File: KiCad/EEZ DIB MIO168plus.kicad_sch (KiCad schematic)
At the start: 11 parts

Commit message: BOM update
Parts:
- KK1, KK2: LCSC (none) -> C959626
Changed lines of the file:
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@@
 	(title_block
 		(title "${project_name}")
-		(date "2026-07-24")
+		(date "2026-07-25")
 		(rev "${project_version}")
 		(company "${project_creator}")
@@
 			)
 		)
+		(property "LCSC" "C959626"
+			(at 109.22 193.04 0)
+			(hide yes)
+			(show_name no)
+			(do_not_autoplace no)
+			(effects
+				(font
+					(size 0.889 0.889)
+				)
+			)
+		)
 		(instances
 			(project "EEZ DIB MIO168plus"
@@
 				)
 			)
+		)
+		(property "LCSC" "C959626"
+			(at 121.92 193.04 0)
+			(hide yes)
+			(show_name no)
+			(do_not_autoplace no)
+			(effects
+				(font
+					(size 0.889 0.889)
+				)
+			)

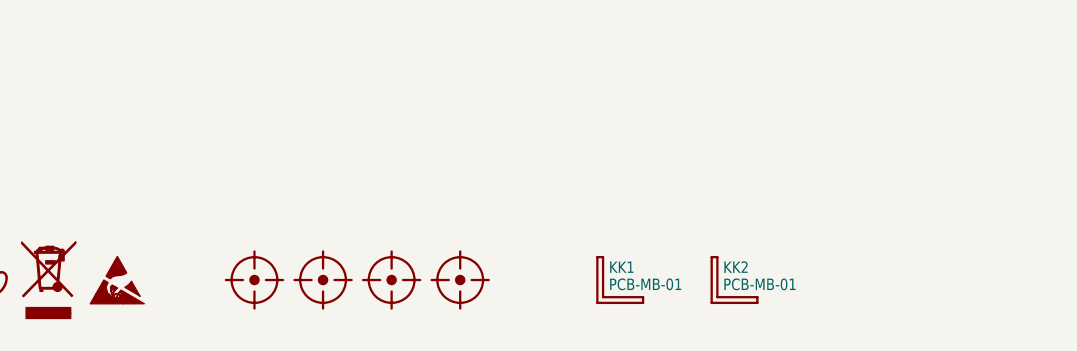
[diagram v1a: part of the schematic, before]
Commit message: OSHWA ID added
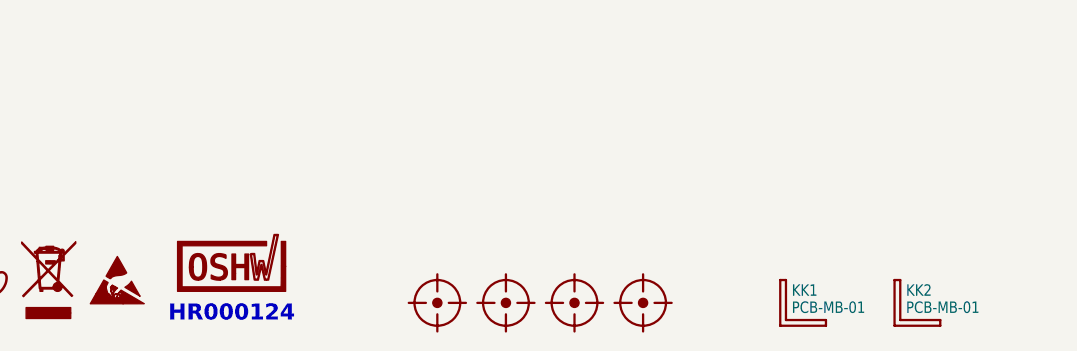
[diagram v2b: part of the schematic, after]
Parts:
- added LOGO7: OSHWA logo, PCM_EEZ_unsorted:OSHWA logo 6.6mm, symbol PCM_EEZ_symbols:OSHWA logo
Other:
- note added: "HR000124"
- moved on the sheet: KK1, KK2
